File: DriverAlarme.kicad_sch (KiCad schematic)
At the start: 18 parts, among them J1 Terminal_Fonte, J2 Terminal_Cerca, J3 Terminal_Alarme, Q1 2N3906, Q2 2N3906

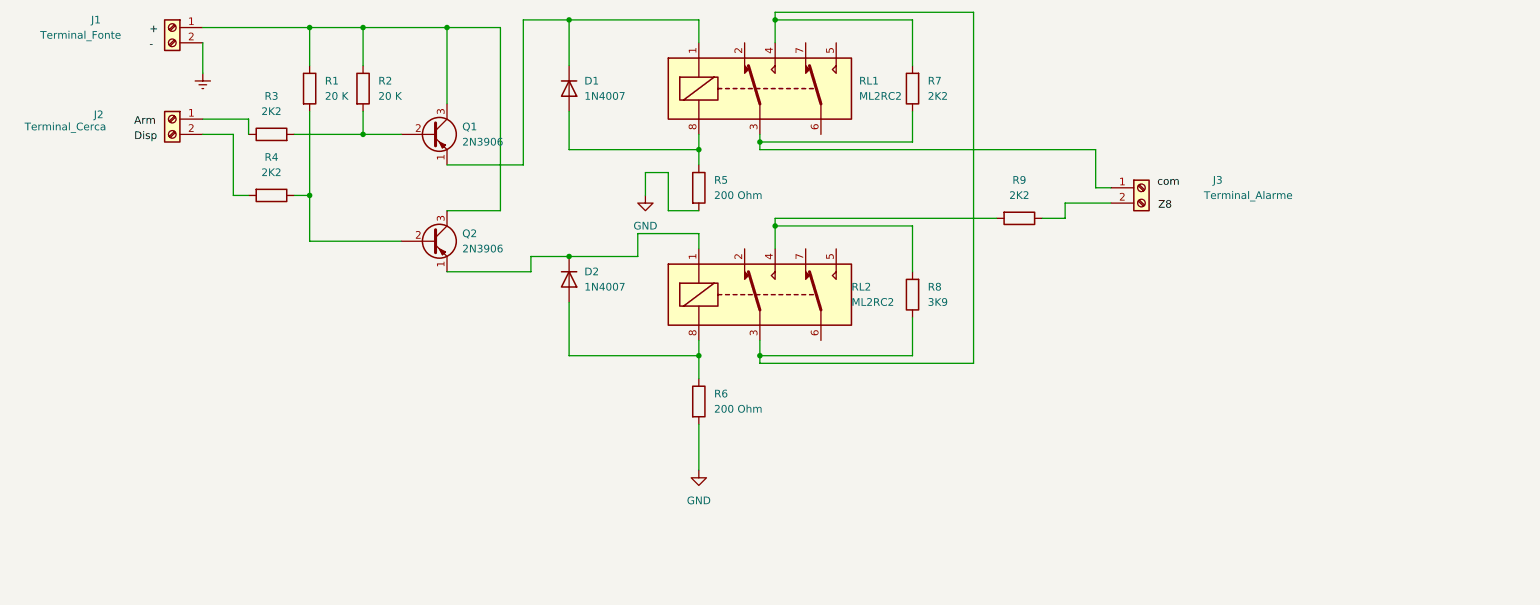
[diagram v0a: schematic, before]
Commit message: Trimpot for adjust current over transistor
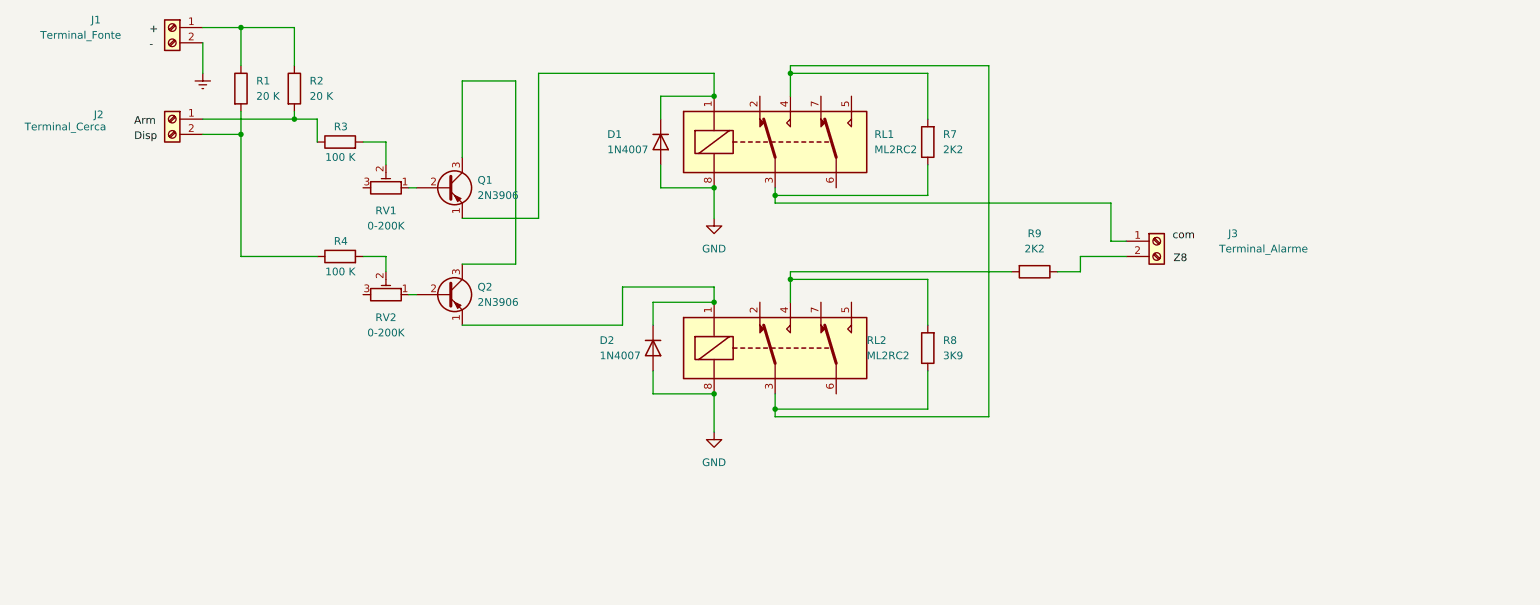
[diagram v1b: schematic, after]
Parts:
- removed R5, R6: 200 Ohm, Resistor_THT:R_Axial_DIN0204_L3.6mm_D1.6mm_P7.62mm_Horizontal, symbol Device:R
- added RV1, RV2: 0-200K, Potentiometer_THT:Potentiometer_Bourns_3386F_Vertical, symbol Device:R_Potentiometer_Trim
- R3, R4: value 2K2 -> 100 K
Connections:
- net GND: now also D1.2 (A), D2.2 (A), RL1.8, RL2.8
- net at J1.1 (Pin_1), R1.1, R2.1: no longer Q1.3 (C), Q2.3 (C)
- net at R1.2, R4.1: now also J2.2 (Pin_2); no longer Q2.2 (B)
- net at J2.1 (Pin_1), R3.1: now also R2.2
- net at R4.2: now also RV2.2; no longer J2.2 (Pin_2)
- new net: R3.2, RV1.2
- new net: Q1.2 (B), RV1.1
- new net: Q2.2 (B), RV2.1
- new net: Q1.3 (C), Q2.3 (C)
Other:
- moved on the sheet: D1, D2, J3, Q1, Q2, R1, R2, R7, R8, R9, RL1, RL2

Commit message: Changed to wired conector
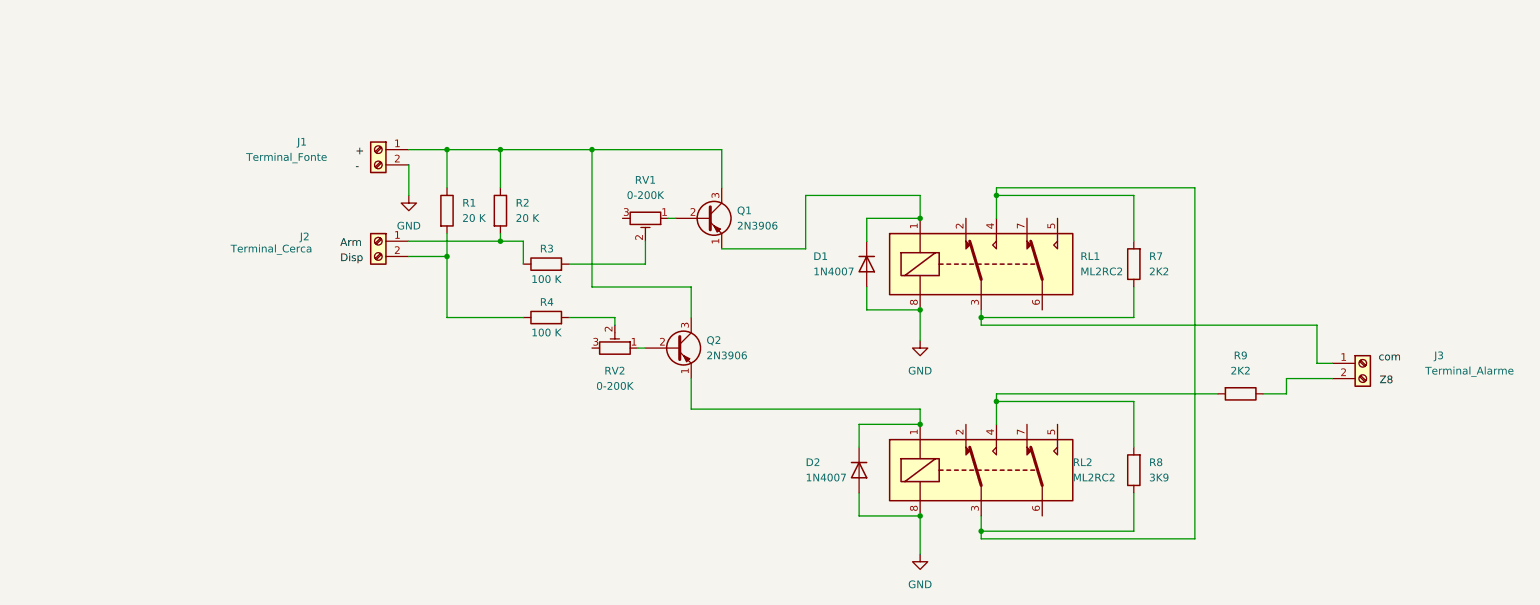
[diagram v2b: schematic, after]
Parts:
- J1, J2, J3: footprint Connector_Phoenix_MC_HighVoltage:PhoenixContact_MC_1,5_2-G-5.08_1x02_P5.08mm_Horizontal -> Connector_Wire:SolderWire-1sqmm_1x02_P5.4mm_D1.4mm_OD2.7mm
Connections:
- net Earth is gone; now on net GND: J1.2 (Pin_2)
- net at J1.1 (Pin_1), R1.1, R2.1: now also Q1.3 (C), Q2.3 (C)
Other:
- moved on the sheet: D1, D2, J1, J2, J3, Q1, Q2, R1, R2, R3, R4, R7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
